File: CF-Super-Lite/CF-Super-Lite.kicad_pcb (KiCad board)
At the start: 2 copper layers, 99.9 x 99.9 mm, 16 parts, among them J1 IDE_CONNECTOR, J2 CF Adapter Power, J3 Bus_ISA_8bit, SW1 DIP Switch x3 or x4, U1 BIOS FLASH, U2 74HCT245, U3 GAL16V8

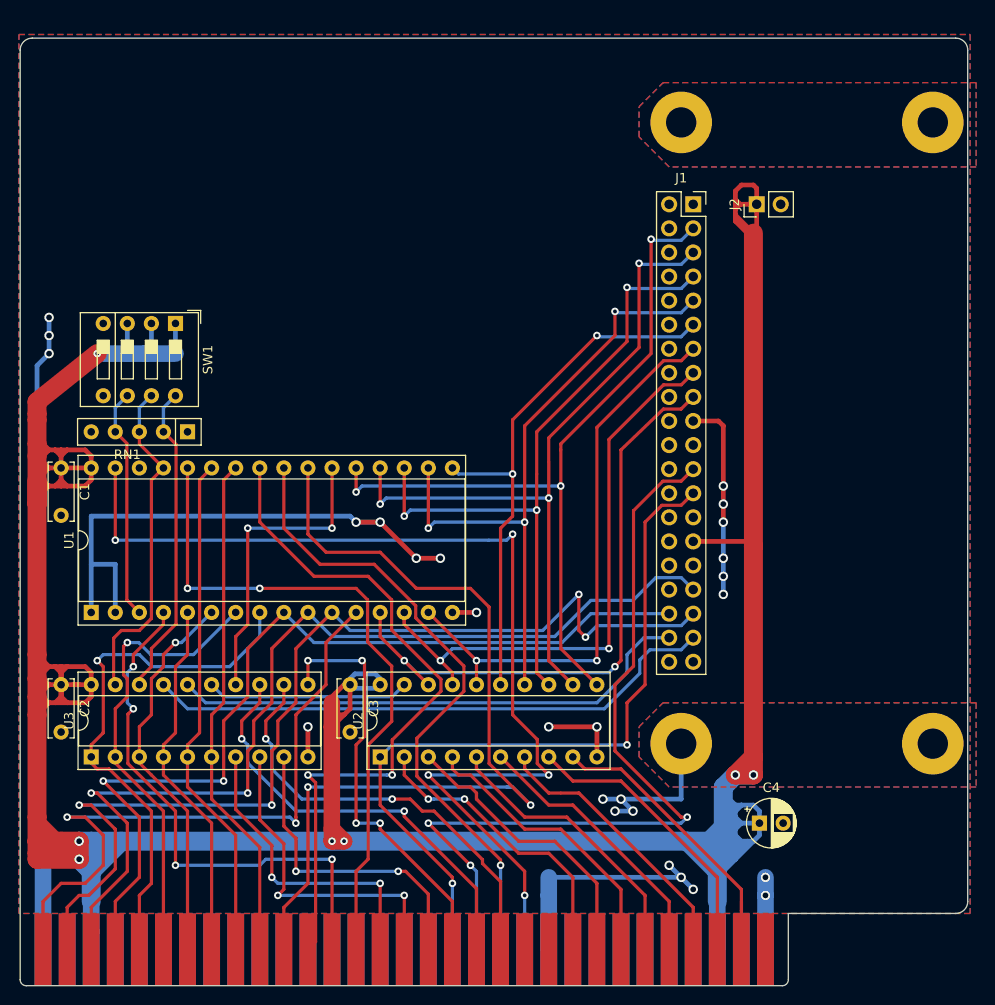
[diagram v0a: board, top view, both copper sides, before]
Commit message: Removed /CS3 output from GAL as XT-IDE doesn't seem to use it. Wemoved A14 to GAL meaning BIOS now has a 32k range in memory rather than 16k. Used freed pins to implement RESET inversion.
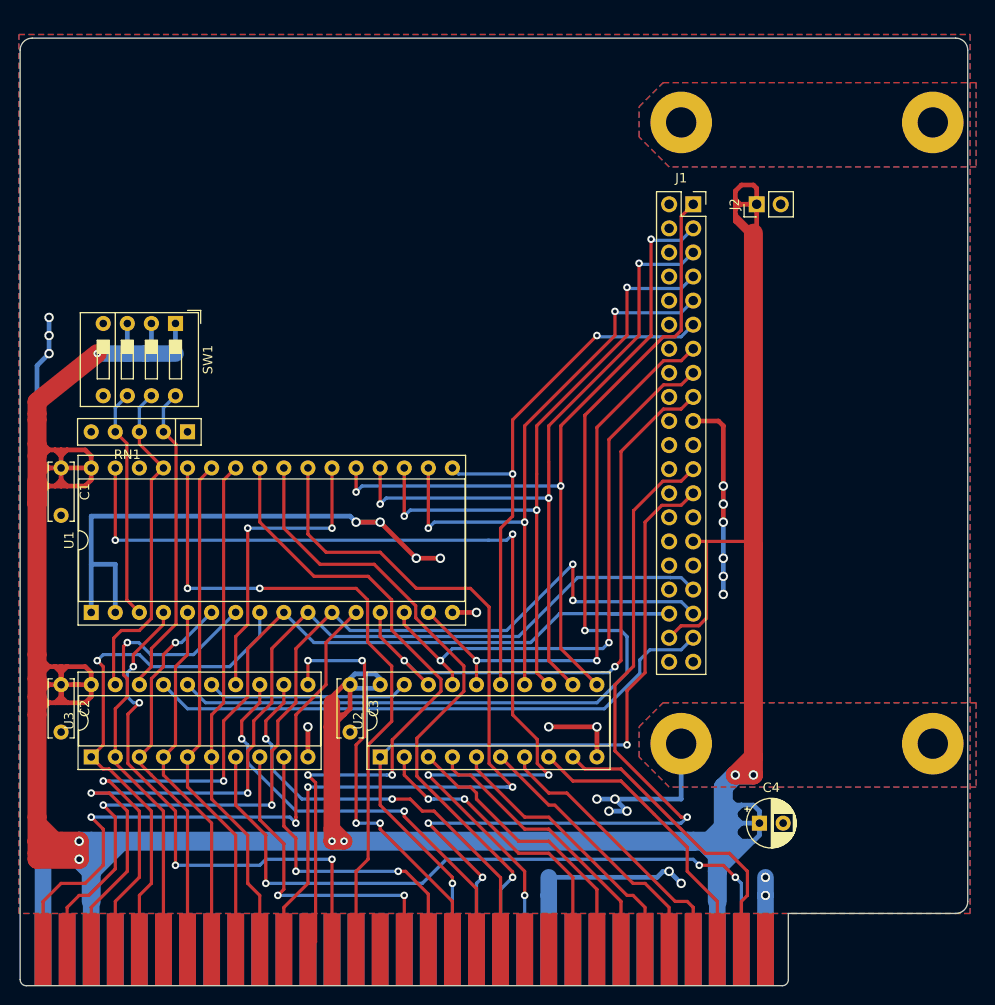
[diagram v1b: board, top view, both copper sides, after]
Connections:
- J1 pad 37: ~CS0~_ATA -> ~CS1~_ATA
- J1 pad 38: ~CS1~_ATA -> VCC
- J3 pad 48: A14 -> Net-(J3-Pad48)
- U3 pad 16: ~CS1~_ATA -> ~RESET
- U3 pad 17: ~CS0~_ATA -> ~CS1~_ATA
- U3 pad 7: A14 -> RESET
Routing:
- net ~RESET: track 0.00 -> 107.4 mm, vias 0 -> 1
- net RESET: track 0.00 -> 73.9 mm, vias 0 -> 3
- net ~CS0~_ATA: track 60.9 -> 0.00 mm
- net A14: track 33.0 -> 0.00 mm, vias 2 -> 0
- net VCC: track 463.6 -> 480.2 mm
- net A03: track 96.7 -> 110.1 mm
- net A10: track 95.1 -> 89.7 mm
- net ~CS1~_ATA: track 55.5 -> 60.9 mm
- net A00: track 70.0 -> 65.3 mm
- net A01: track 109.1 -> 105.4 mm
- net GND: track 212.2 -> 210.0 mm, vias 26 -> 25
- net D7: track 29.9 -> 31.9 mm
- net ~MEMR: track 67.7 -> 68.8 mm
- net A12: track 57.1 -> 58.0 mm
- net A02: track 103.0 -> 103.8 mm
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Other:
- net class Power: clearance 0.25 -> 0.24

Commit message: CF-Super-Lite: Final board tweaks before sending to production.
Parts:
- SW1: value DIP Switch x3 or x4 -> DIP Switch
- moved SW1 10.8 mm to (105.4, 80.0), turned to 90 degrees
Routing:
- net ROM_ADDR_JUMPER: track 33.2 -> 49.5 mm
- net VCC: track 480.2 -> 464.5 mm
- net V20_JUMPER: track 24.4 -> 36.8 mm
- net ATA_ADDR_JUMPER: track 35.4 -> 43.0 mm
- net D0: track 31.8 -> 29.9 mm
- net D1: track 30.3 -> 29.2 mm
- net A15: track 35.0 -> 34.4 mm
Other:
- board text added: "8086/8088"
- board text added: "BUSSED"
- board text added: "Copyright (C) 2021 Titanium Studios Pty Ltd"
- board text added: "PORT 300h"
- board text added: "Port 320h"
- board text added: "ROM C800h"
- board text added: "ROM D800h"
- board text added: "SST39SF010, SST39SF020, SST39SF040 or similar"
- board text added: "UNUSED"
- board text added: "V20, 286,..."
- board text added: "XTIDE CF Super-Lite"
- board text added: "https://github.com/JayesonLS/ ISA-Cards/tree/master/CF-Super-Lite"

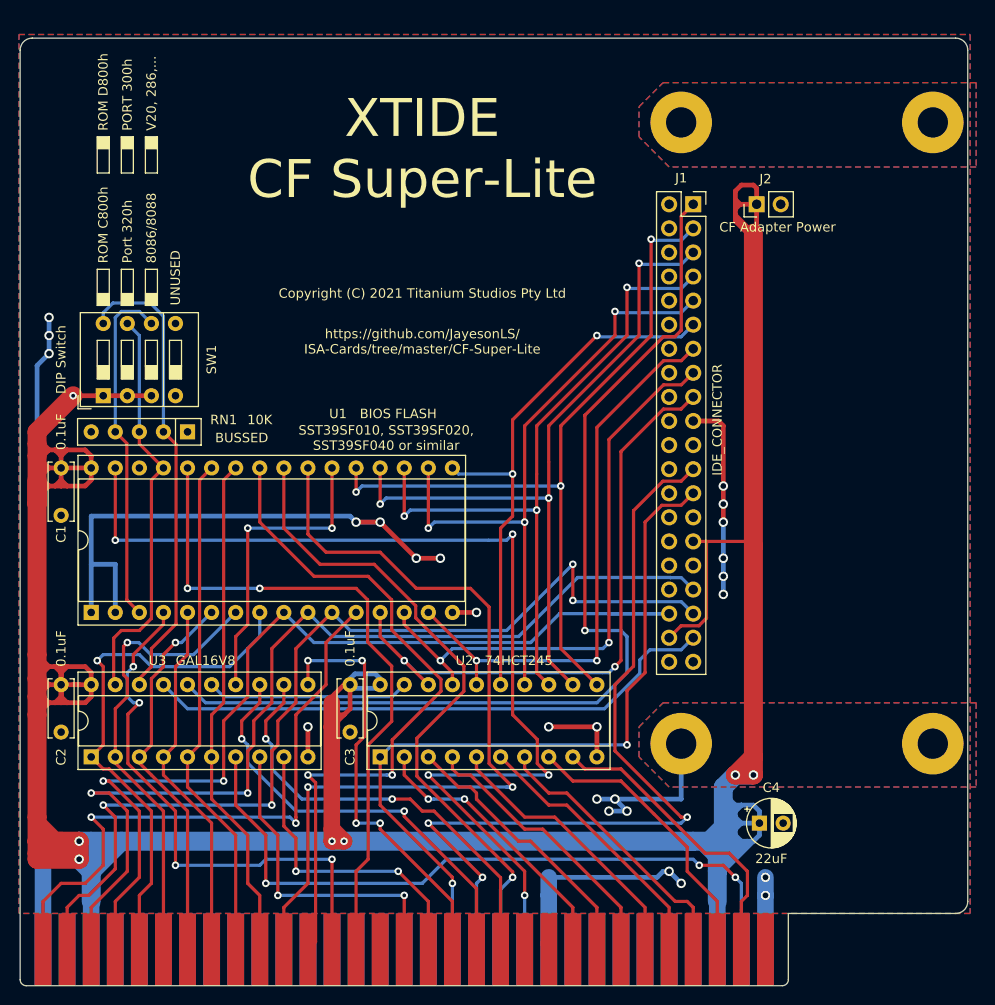
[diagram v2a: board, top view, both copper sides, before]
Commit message: CF-Super-Lite: Swap 16v8 GAL  for 22v10, add signals to generate correct buffer direction.
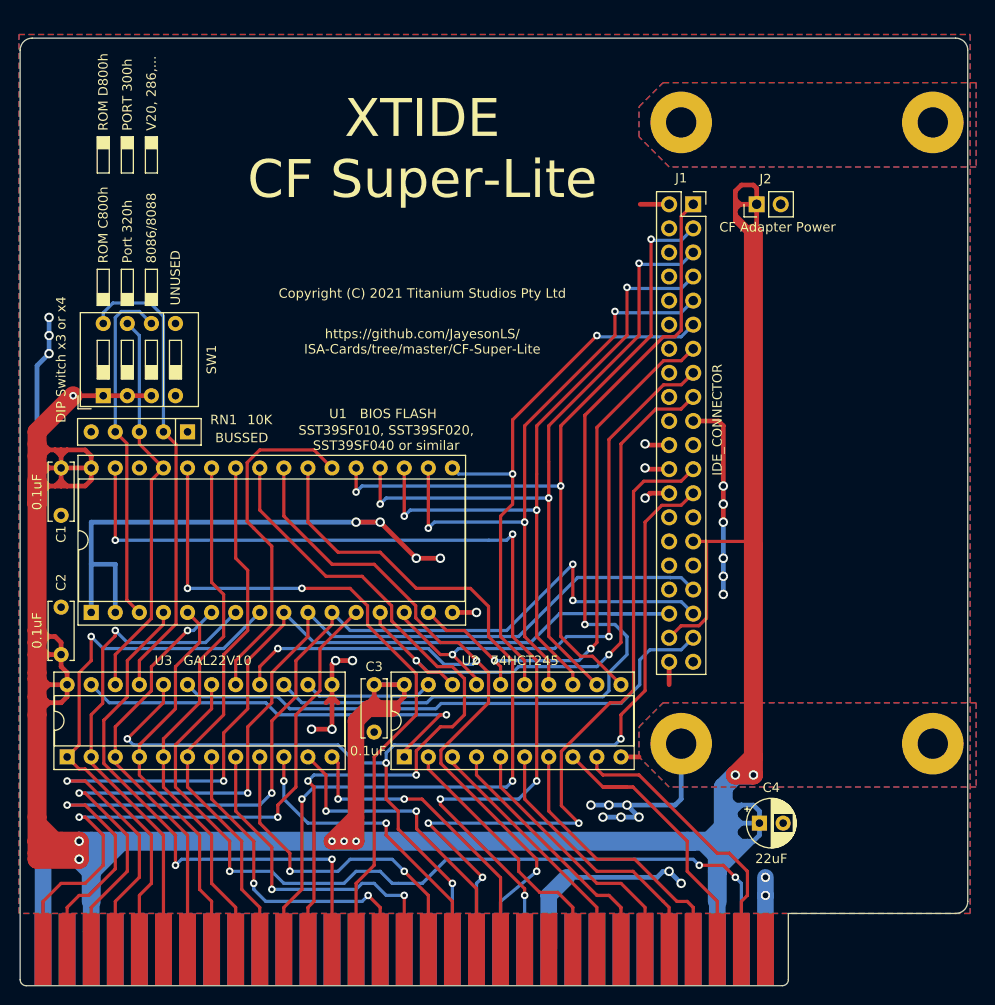
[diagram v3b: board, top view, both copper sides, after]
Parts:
- SW1: value DIP Switch -> DIP Switch x3 or x4
- U3: value GAL16V8 -> GAL22V10; footprint Package_DIP:DIP-20_W7.62mm_Socket -> Package_DIP:DIP-24_W7.62mm_Socket
- moved C2 3.17 mm to (101.0, 107.3), turned to 90 degrees
- moved C3 2.54 mm to (134.0, 110.5)
- moved U3 2.54 mm to (101.6, 118.1)
- moved U2 2.54 mm to (137.2, 118.1)
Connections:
- J3 pad 48: Net-(J3-Pad48) -> A14
- U2 pad 1: ~IOR -> ~IOR_OR_MEMR
- U3 pad 10: GND -> A17
- U3 pad 11: A17 -> A18
- U3 pad 13: A18 -> GND
- U3 pad 14: ~CE~_BIOS -> ~CE~_D_BUF
- U3 pad 15: ~CE~_D_BUF -> ~RESET
- U3 pad 16: ~RESET -> ~MEMR
- U3 pad 17: ~CS1~_ATA -> ~CE~_BIOS
- U3 pad 18: ROM_ADDR_JUMPER -> RESET
- U3 pad 19: ATA_ADDR_JUMPER -> ~CS1~_ATA
- U3 pad 20: VCC -> ~IOR
- U3 pad 7: RESET -> A14
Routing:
- net ~IOR_OR_MEMR: track 0.00 -> 45.4 mm, vias 0 -> 1
- net A14: track 0.00 -> 34.9 mm, vias 0 -> 2
- net ~IOR: track 80.7 -> 114.9 mm, vias 2 -> 4
- net ~MEMR: track 68.8 -> 97.9 mm, vias 1 -> 3
- net GND: track 210.0 -> 227.8 mm, vias 25 -> 31
- net RESET: track 73.9 -> 88.3 mm
- net A19: track 46.4 -> 32.9 mm
- net A18: track 45.7 -> 33.3 mm
- net A17: track 44.9 -> 32.5 mm, vias 4 -> 2
- net ~RESET: track 107.4 -> 96.8 mm
- net ~IOW: track 88.3 -> 78.7 mm
- net ~CE~_D_BUF: track 21.4 -> 13.7 mm
- net A03: track 110.1 -> 116.2 mm
- net A01: track 105.4 -> 111.1 mm
- net VCC: track 464.5 -> 458.9 mm, vias 7 -> 8
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
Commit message: CF-Super-Lite: Swap dip switch and resistor array for jumper block.
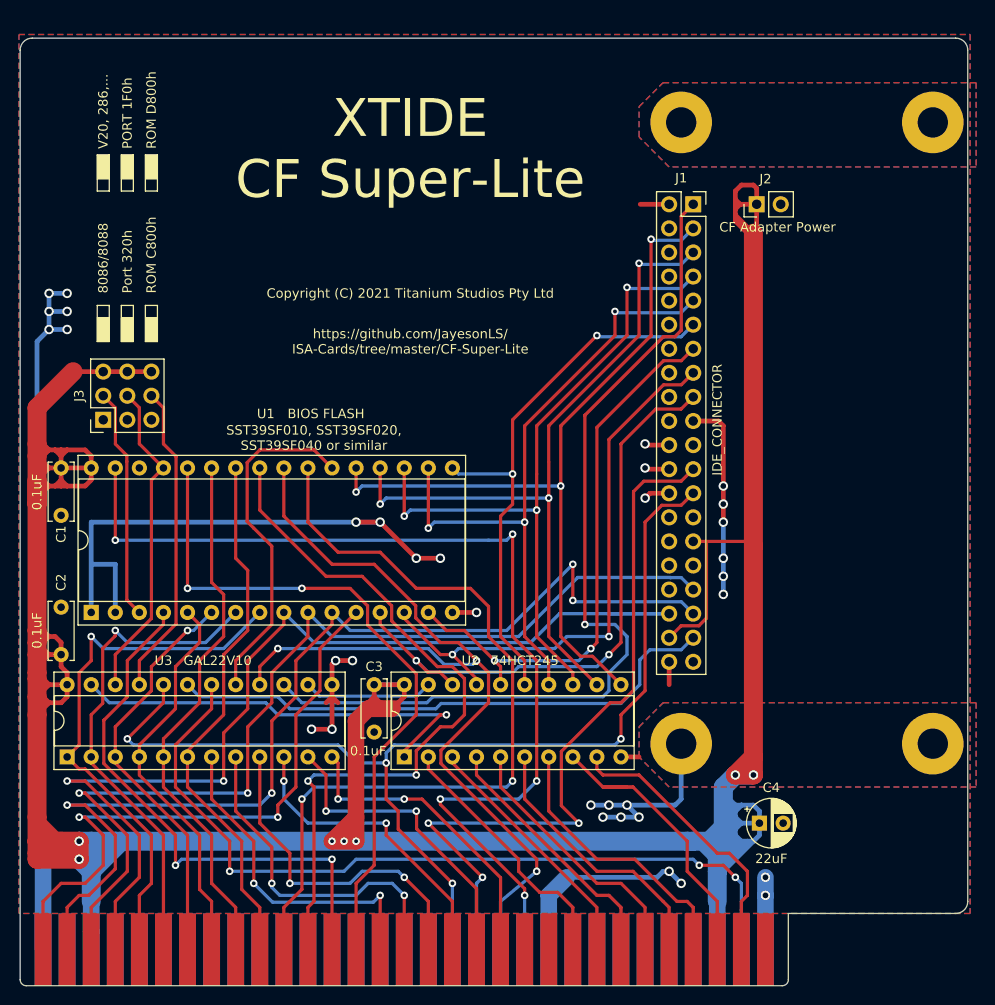
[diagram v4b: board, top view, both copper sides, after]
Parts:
- removed RN1: 10K, Resistor_THT:R_Array_SIP5
- removed SW1: DIP Switch x3 or x4, Button_Switch_THT:SW_DIP_SPSTx04_Slide_9.78x12.34mm_W7.62mm_P2.54mm
- added J3: Jumpers, 00Custom:PinHeader_3x03_P2.54mm_Vertical, F.Cu at (105.4, 82.5)
- renumbered J3 to J4
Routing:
- net ROM_ADDR_JUMPER: track 50.1 -> 33.8 mm
- net V20_JUMPER: track 36.8 -> 24.4 mm
- net GND: track 227.8 -> 236.1 mm, vias 31 -> 34
- net ATA_ADDR_JUMPER: track 42.0 -> 34.4 mm
- net VCC: track 458.9 -> 461.4 mm, vias 8 -> 7
- net RESET: track 88.3 -> 86.2 mm
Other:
- board text added: "PORT 1F0h"
- board text removed: "BUSSED"
- board text removed: "PORT 300h"
- board text removed: "UNUSED"

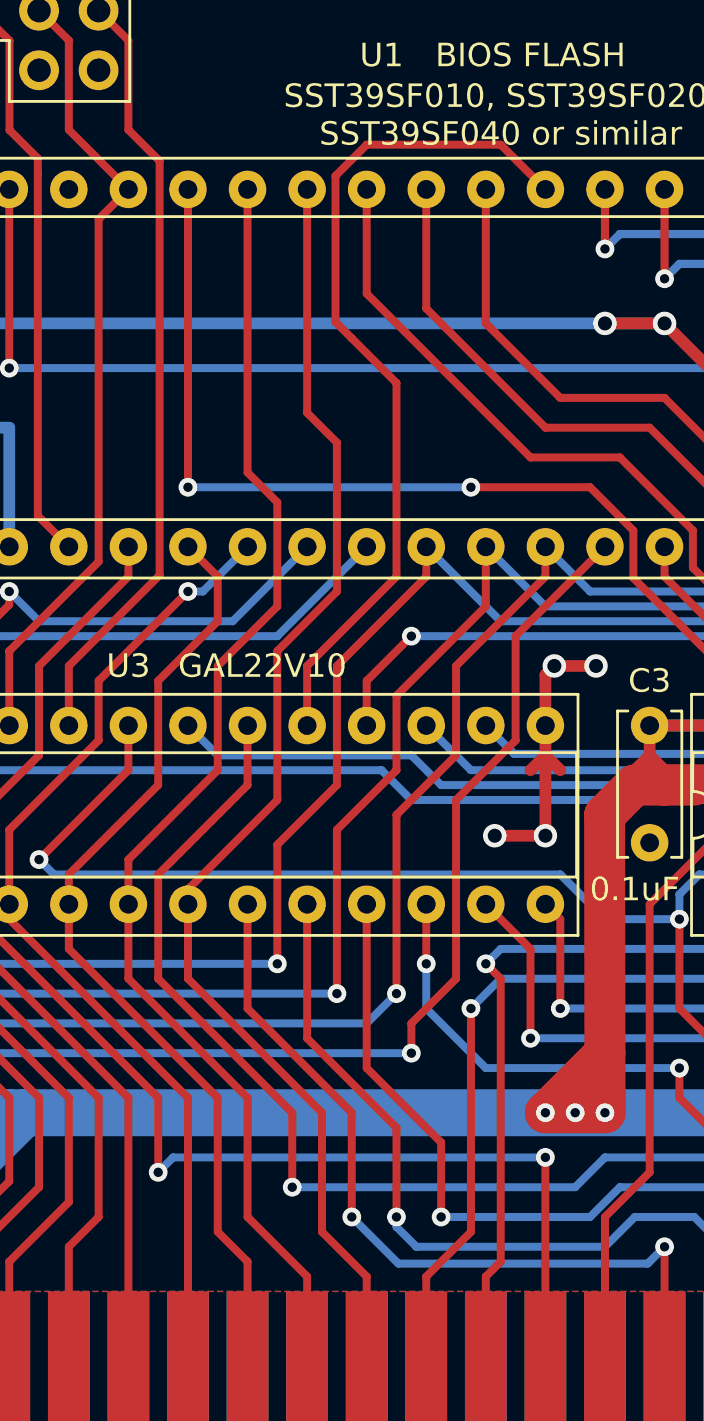
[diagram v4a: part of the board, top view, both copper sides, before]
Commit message: CF-Super-Line: Swap two GAL pins to match CD-Clock-Combo.
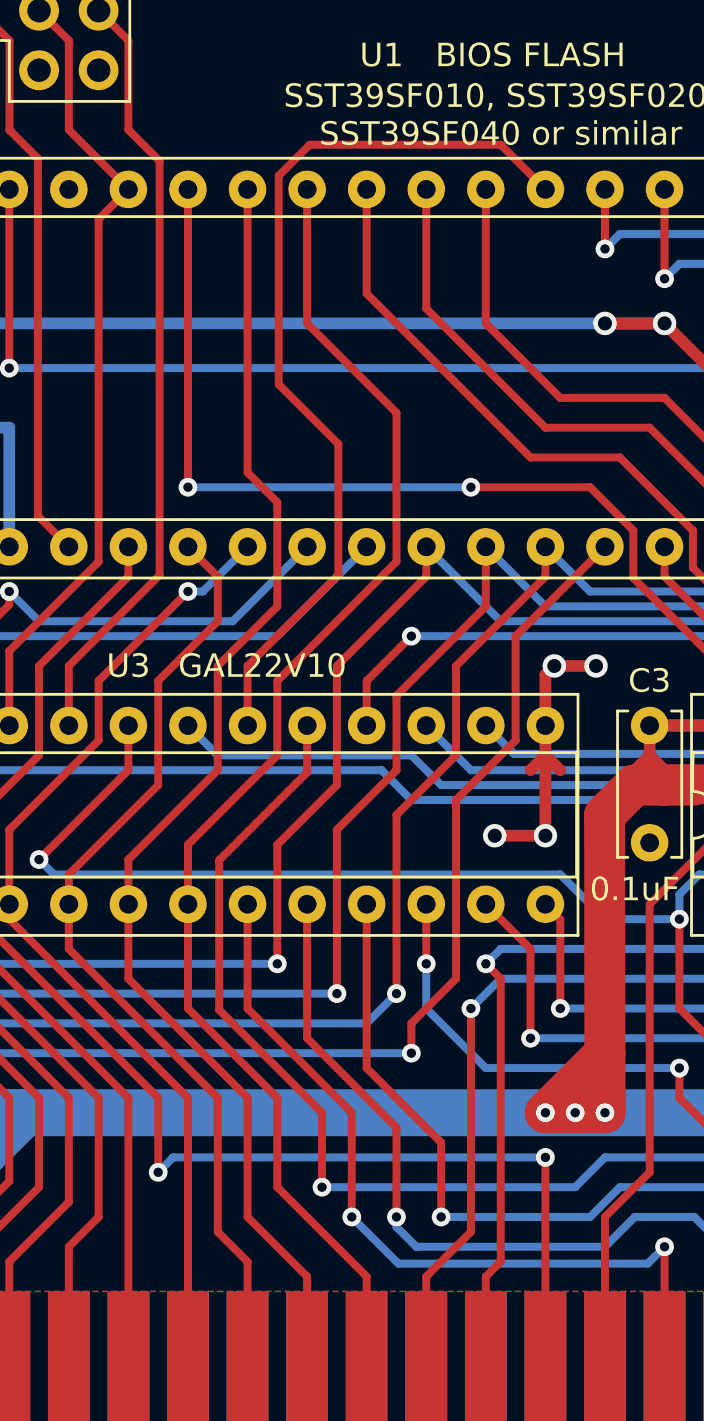
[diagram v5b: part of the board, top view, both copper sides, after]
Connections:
- U3 pad 17: ~CE~_BIOS -> RESET
- U3 pad 18: RESET -> ~CE~_BIOS
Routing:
- net ~CE~_BIOS: track 36.4 -> 38.8 mm
- net A09: track 57.1 -> 59.2 mm
- net RESET: track 86.2 -> 84.3 mm

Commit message: Fix location of CF adapter power for all boards that use it. Also the mounting holes in the schematic for the same boards. Finishing touches to Tandy 1000 Essentials.
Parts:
- J2: footprint Connector_PinHeader_2.54mm:PinHeader_1x02_P2.54mm_Vertical -> Connector_PinSocket_2.54mm:PinSocket_1x01_P2.54mm_Vertical
- moved J2 7.62 mm to (182.0, 59.8)
- renumbered MH1 to H1, MH2 to H2, MH3 to H3, MH4 to H4
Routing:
- net VCC: track 461.4 -> 462.5 mm
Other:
- board text added: "https://github.com/JayesonLS/ISA-Cards"
- board text removed: "https://github.com/JayesonLS/ ISA-Cards/tree/master/CF-Super-Lite"
